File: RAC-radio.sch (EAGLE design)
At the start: 1 part, among them IC1 RN4871-I_RM130

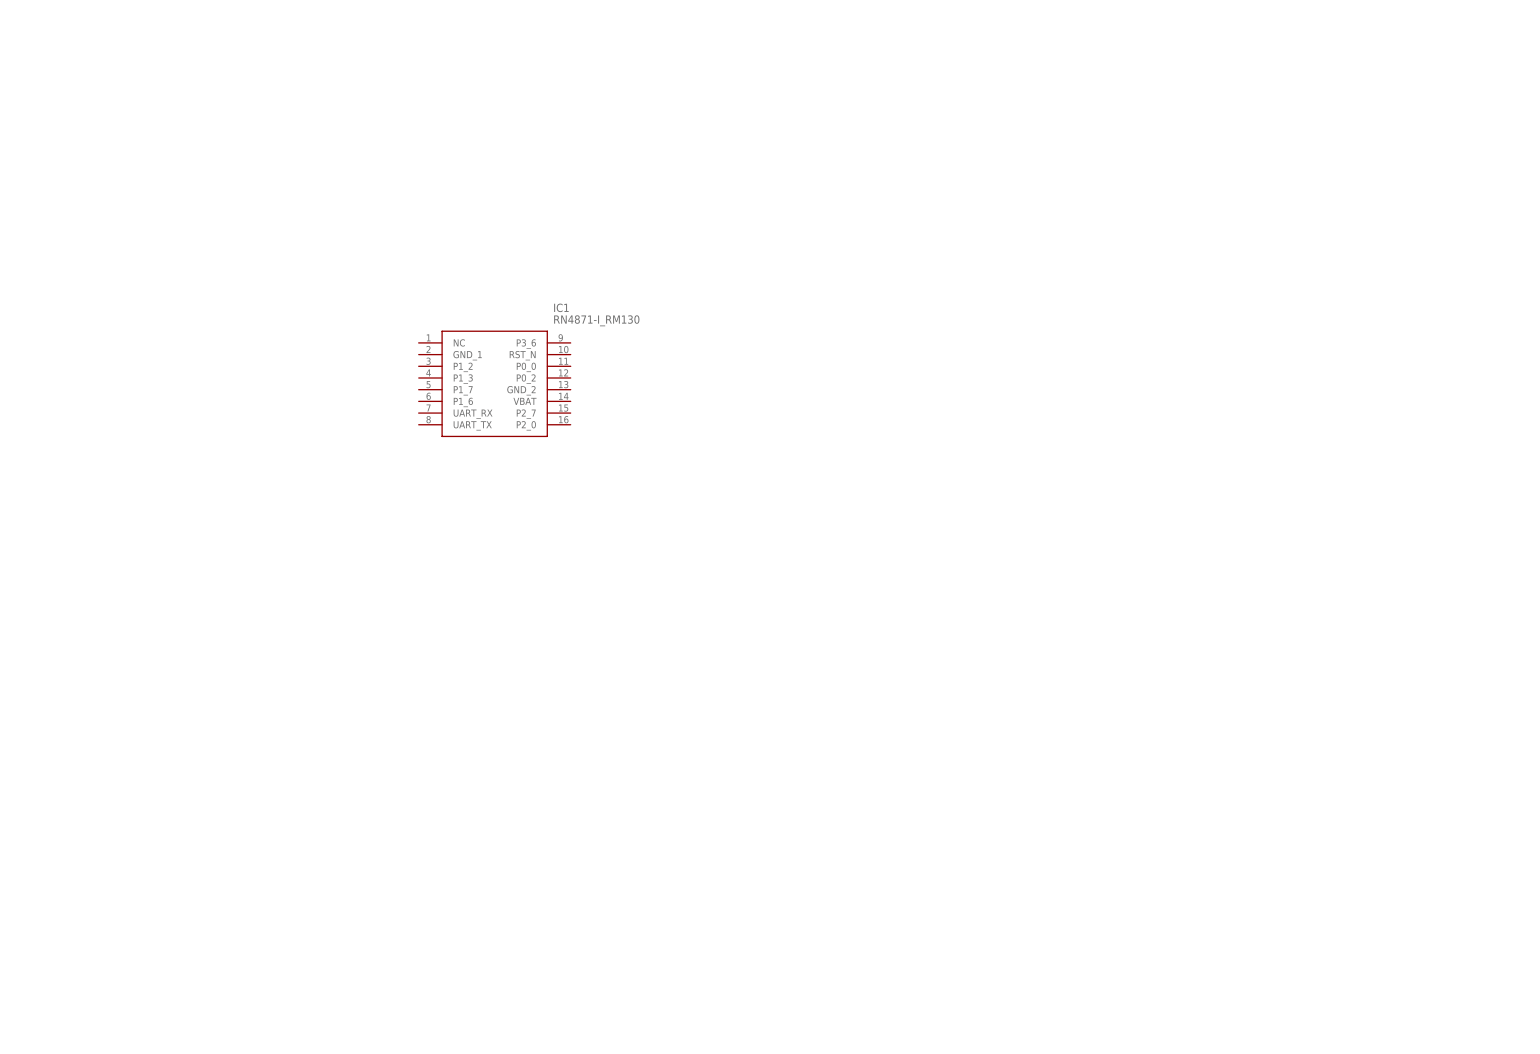
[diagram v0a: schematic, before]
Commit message: Integrated MCU, BLE, and LoRa subsystems
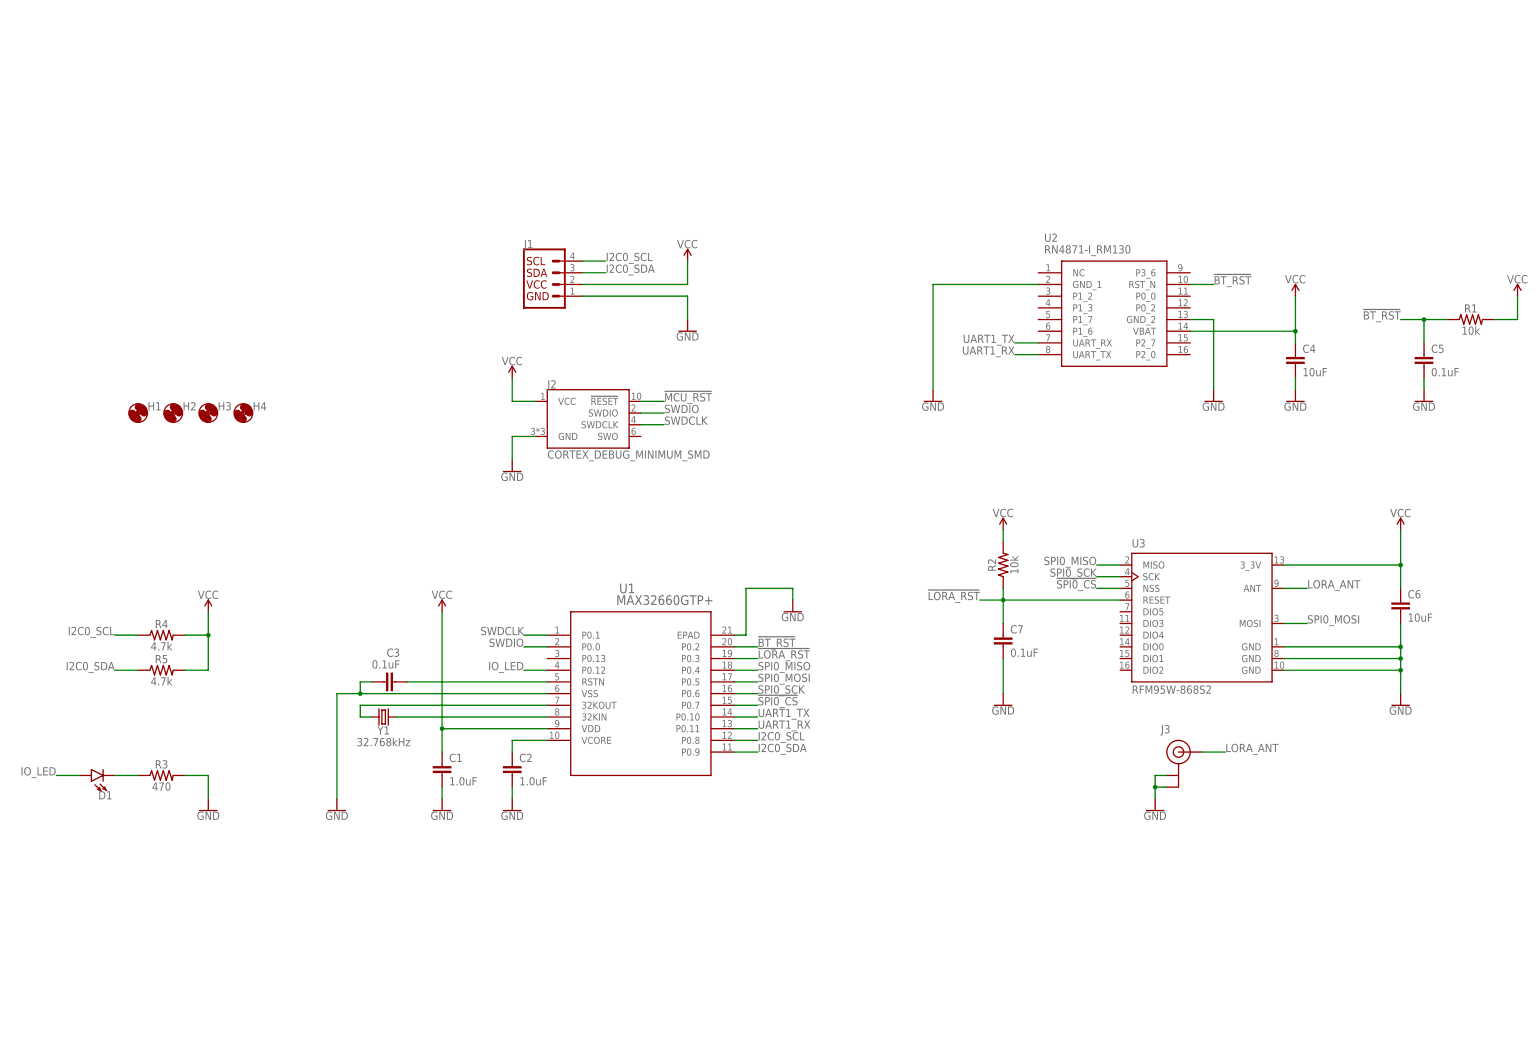
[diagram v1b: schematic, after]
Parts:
- removed IC1: RN4871-I_RM130, RAC-Altimeter:RN4871-I_RM130
- added C1, C2: 1.0uF, SparkFun-Capacitors:1.0UF-0603-16V-10%
- added C3, C5, C7: 0.1uF, SparkFun-Capacitors:0.1UF-0603-25V-(+80/-20%)
- added C4, C6: 10uF, SparkFun-Capacitors:10UF-0603-6.3V-20%
- added D1: (no value), SparkFun-LED:LED0603
- added H1, H2, H3, H4: MOUNT-HOLE2.8, holes:MOUNT-HOLE2.8
- added J1: (no value), SparkFun-Connectors:QWIIC_CONNECTORJS-1MM
- added J2: CORTEX_DEBUG_MINIMUM_SMD, SparkFun-Connectors:CORTEX_DEBUG_MINIMUM_SMD
- added J3: U.FL, SparkFun-Connectors:U.FL
- added R1, R2: 10k, SparkFun-Resistors:10KOHM-0603-1/10W-1%
- added R3: 470, SparkFun-Resistors:470OHM-0603-1/10W-1%
- added R4, R5: 4.7k, SparkFun-Resistors:4.7KOHM-0603-1/10W-1%
- added U1: MAX32660GTP+, RAC-Altimeter:MAX32660GTP+
- added U2: RN4871-I_RM130, RAC-Altimeter:RN4871-I_RM130
- added U3: RFM95W-868S2, RAC-Altimeter:RFM95W-868S2
- added Y1: 32.768kHz, SparkFun-Clocks:CRYSTAL-32.768KHZSMD-3.2X1.5
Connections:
- new net !BT_RST: C5.1, R1.1, U1.P0.2, U2.RST_N
- new net !LORA_RST: C7.1, R2.1, U1.P0.3, U3.RESET
- new net !MCU_RST: C3.1, J2.!RESET, U1.RSTN
- new net !SPI0_CS: U1.P0.7, U3.NSS
- new net 32KIN: U1.32KIN, Y1.1
- new net 32KOUT: U1.32KOUT, Y1.2
- new net GND: C1.2, C2.2, C3.2, C4.2, C5.2, C6.2, C7.2, J1.1, J2.GND, J3.GND@0, J3.GND@1, R3.2, U1.EPAD, U1.VSS, U2.GND_1, U2.GND_2, U3.GND, U3.GND@1, U3.GND@2
- new net I2C0_SCL: J1.4, R4.1, U1.P0.8
- new net I2C0_SDA: J1.3, R5.1, U1.P0.9
- new net IO_LED: D1.A, U1.P0.12
- new net LORA_ANT: J3.SIGNAL, U3.ANT
- new net N$2: D1.C, R3.1
- new net SPI0_MISO: U1.P0.4, U3.MISO
- new net SPI0_MOSI: U1.P0.5, U3.MOSI
- new net SPI0_SCK: U1.P0.6, U3.SCK
- new net SWDCLK: J2.SWDCLK, U1.P0.1
- new net SWDIO: J2.SWDIO, U1.P0.0
- new net UART1_RX: U1.P0.11, U2.UART_TX
- new net UART1_TX: U1.P0.10, U2.UART_RX
- new net VCC: C1.1, C4.1, C6.1, J1.2, J2.VCC, R1.2, R2.2, R4.2, R5.2, U1.VDD, U2.VBAT, U3.3_3V
- new net VCORE: C2.1, U1.VCORE

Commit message: Routed the non-power nets
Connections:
- net N$2 renamed LED_CATH
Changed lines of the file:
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@@
 </segment>
 </net>
-<net name="N$2" class="0">
+<net name="LED_CATH" class="0">
 <segment>
 <pinref part="D1" gate="G$1" pin="C"/>

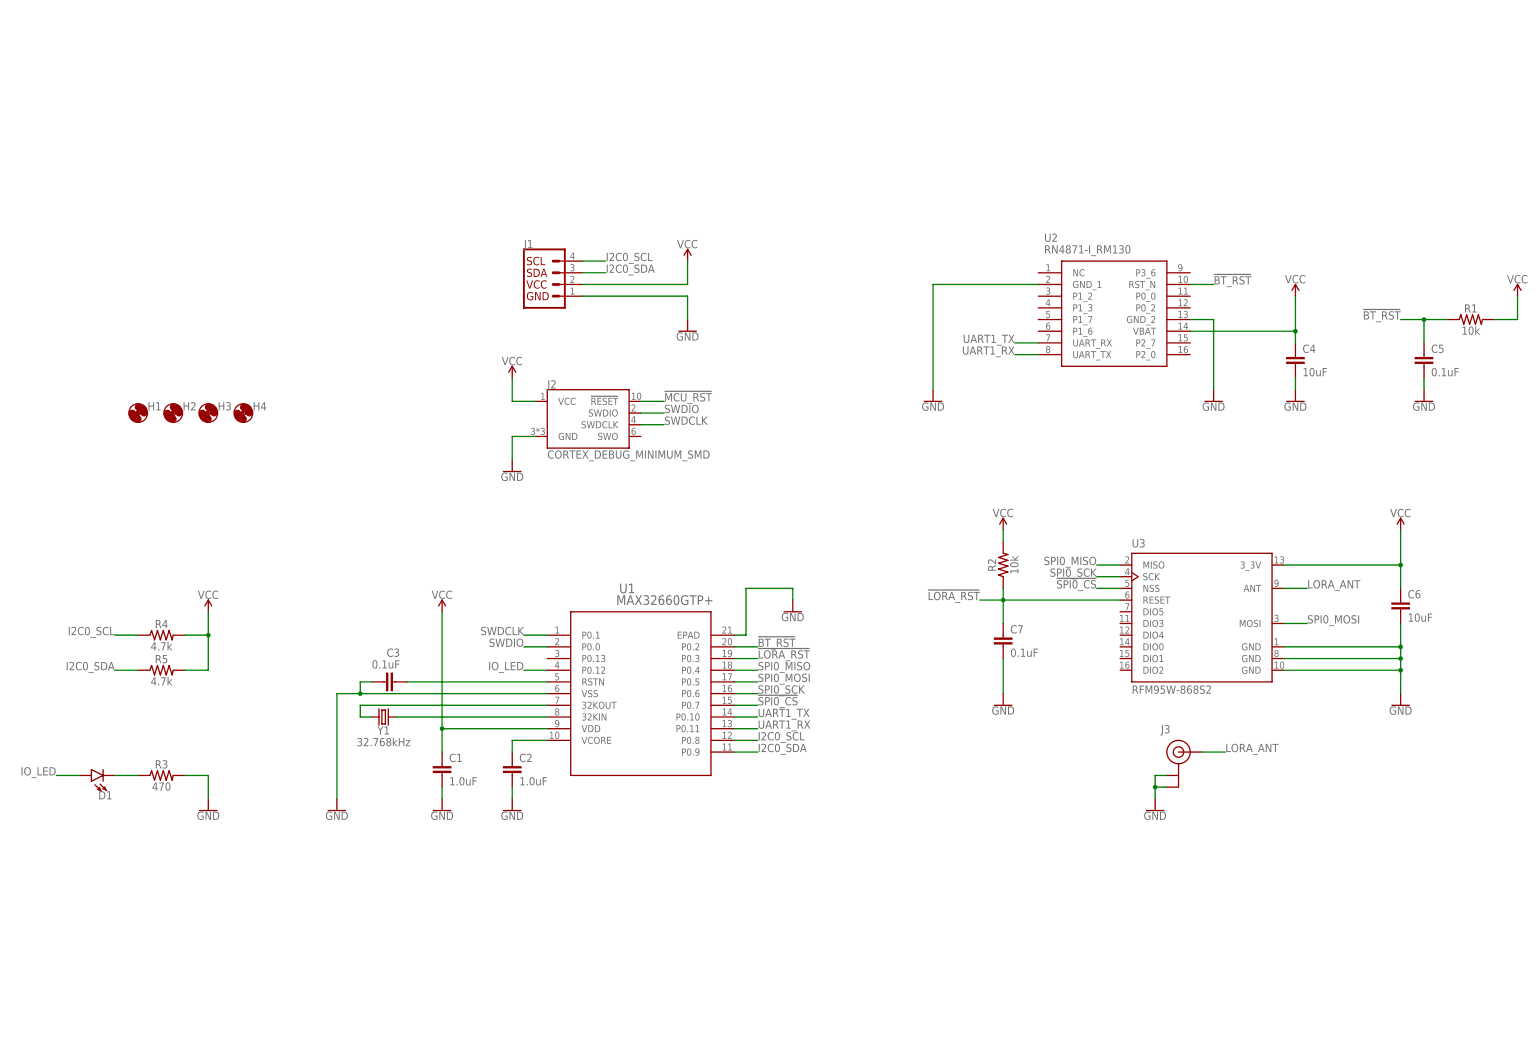
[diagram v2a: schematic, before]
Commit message: Started anew with the SIM7000 LTE-M/GPS module
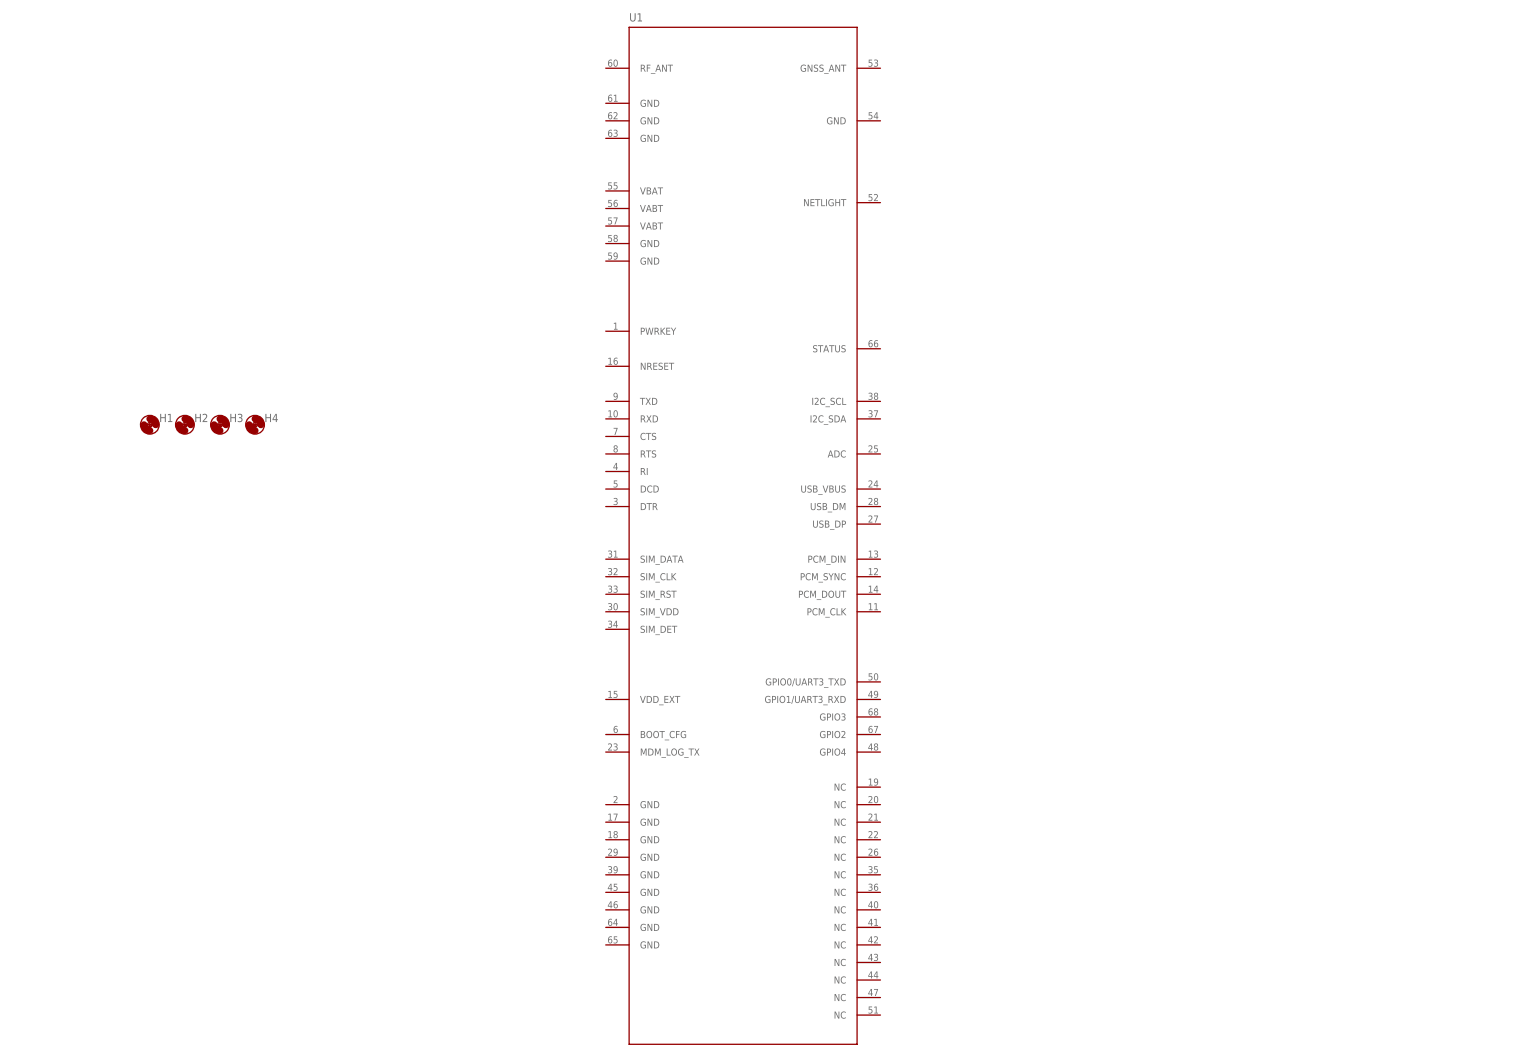
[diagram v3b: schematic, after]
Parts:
- removed C1, C2: 1.0uF, SparkFun-Capacitors:1.0UF-0603-16V-10%
- removed C3, C5, C7: 0.1uF, SparkFun-Capacitors:0.1UF-0603-25V-(+80/-20%)
- removed C4, C6: 10uF, SparkFun-Capacitors:10UF-0603-6.3V-20%
- removed D1: (no value), SparkFun-LED:LED0603
- removed J1: (no value), SparkFun-Connectors:QWIIC_CONNECTORJS-1MM
- removed J2: CORTEX_DEBUG_MINIMUM_SMD, SparkFun-Connectors:CORTEX_DEBUG_MINIMUM_SMD
- removed J3: U.FL, SparkFun-Connectors:U.FL
- removed R1, R2: 10k, SparkFun-Resistors:10KOHM-0603-1/10W-1%
- removed R3: 470, SparkFun-Resistors:470OHM-0603-1/10W-1%
- removed R4, R5: 4.7k, SparkFun-Resistors:4.7KOHM-0603-1/10W-1%
- removed U2: RN4871-I_RM130, RAC-Altimeter:RN4871-I_RM130
- removed U3: RFM95W-868S2, RAC-Altimeter:RFM95W-868S2
- removed Y1: 32.768kHz, SparkFun-Clocks:CRYSTAL-32.768KHZSMD-3.2X1.5
- U1: value MAX32660GTP+ -> (none); device RAC-Altimeter:MAX32660GTP+ -> rocket-components:SIM7000
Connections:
- removed net !BT_RST: C5.1, R1.1, U1.P0.2, U2.RST_N
- removed net !LORA_RST: C7.1, R2.1, U1.P0.3, U3.RESET
- removed net !MCU_RST: C3.1, J2.!RESET, U1.RSTN
- removed net !SPI0_CS: U1.P0.7, U3.NSS
- removed net 32KIN: U1.32KIN, Y1.1
- removed net 32KOUT: U1.32KOUT, Y1.2
- removed net GND: C1.2, C2.2, C3.2, C4.2, C5.2, C6.2, C7.2, J1.1, J2.GND, J3.GND@0, J3.GND@1, R3.2, U1.EPAD, U1.VSS, U2.GND_1, U2.GND_2, U3.GND, U3.GND@1, U3.GND@2
- removed net I2C0_SCL: J1.4, R4.1, U1.P0.8
- removed net I2C0_SDA: J1.3, R5.1, U1.P0.9
- removed net IO_LED: D1.A, U1.P0.12
- removed net LED_CATH: D1.C, R3.1
- removed net LORA_ANT: J3.SIGNAL, U3.ANT
- removed net SPI0_MISO: U1.P0.4, U3.MISO
- removed net SPI0_MOSI: U1.P0.5, U3.MOSI
- removed net SPI0_SCK: U1.P0.6, U3.SCK
- removed net SWDCLK: J2.SWDCLK, U1.P0.1
- removed net SWDIO: J2.SWDIO, U1.P0.0
- removed net UART1_RX: U1.P0.11, U2.UART_TX
- removed net UART1_TX: U1.P0.10, U2.UART_RX
- removed net VCC: C1.1, C4.1, C6.1, J1.2, J2.VCC, R1.2, R2.2, R4.2, R5.2, U1.VDD, U2.VBAT, U3.3_3V
- removed net VCORE: C2.1, U1.VCORE
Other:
- moved on the sheet: H1, H2, H3, H4
